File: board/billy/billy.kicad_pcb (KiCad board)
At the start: 2 copper layers, 70 x 50 mm, 85 parts, among them J1 Screw_Terminal_01x02, J10 Screw_Terminal_01x02, J11 Screw_Terminal_01x03, J12 USB_B_Micro, J2 Conn_01x06, J3 Screw_Terminal_01x02, J4 Screw_Terminal_01x02, J5 Conn_01x02, J6 Conn_01x03, J7 Screw_Terminal_01x06, Q1 AO3401A, Q2 AO3401A, Q4 AO3400A, Q6 AO3400A, Q7 AO3400A, SW1 TS-1088-AR02016, U1 ESP32-S3-WROOM-1, U2 DRV8833PWPR, U3 MAX98357A, U4 DRV8833PWPR, U5 LTC4412, U6 AP63203WU, U7 USBLC6-2SC6

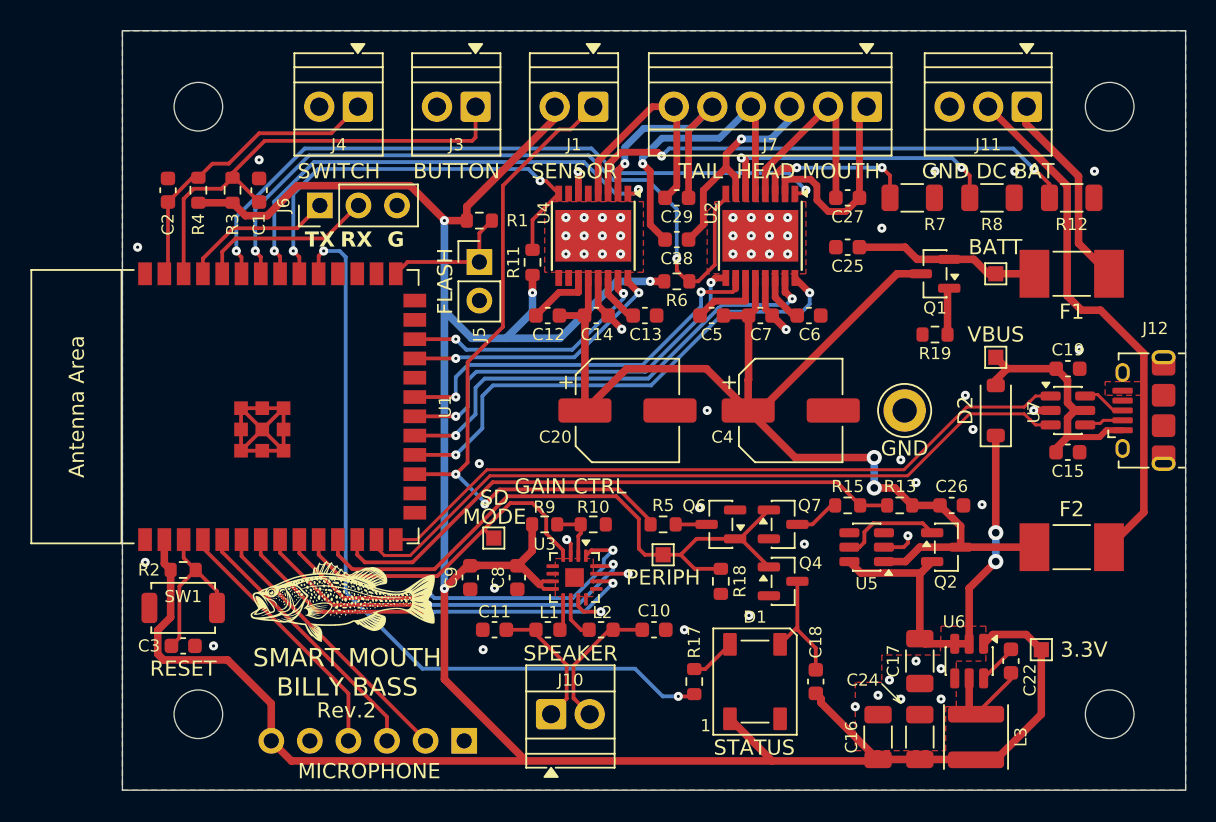
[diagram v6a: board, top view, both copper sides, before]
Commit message: Fix D2 footprint to SOD-323 (was SOD-123) and remove unused test points for rev.2
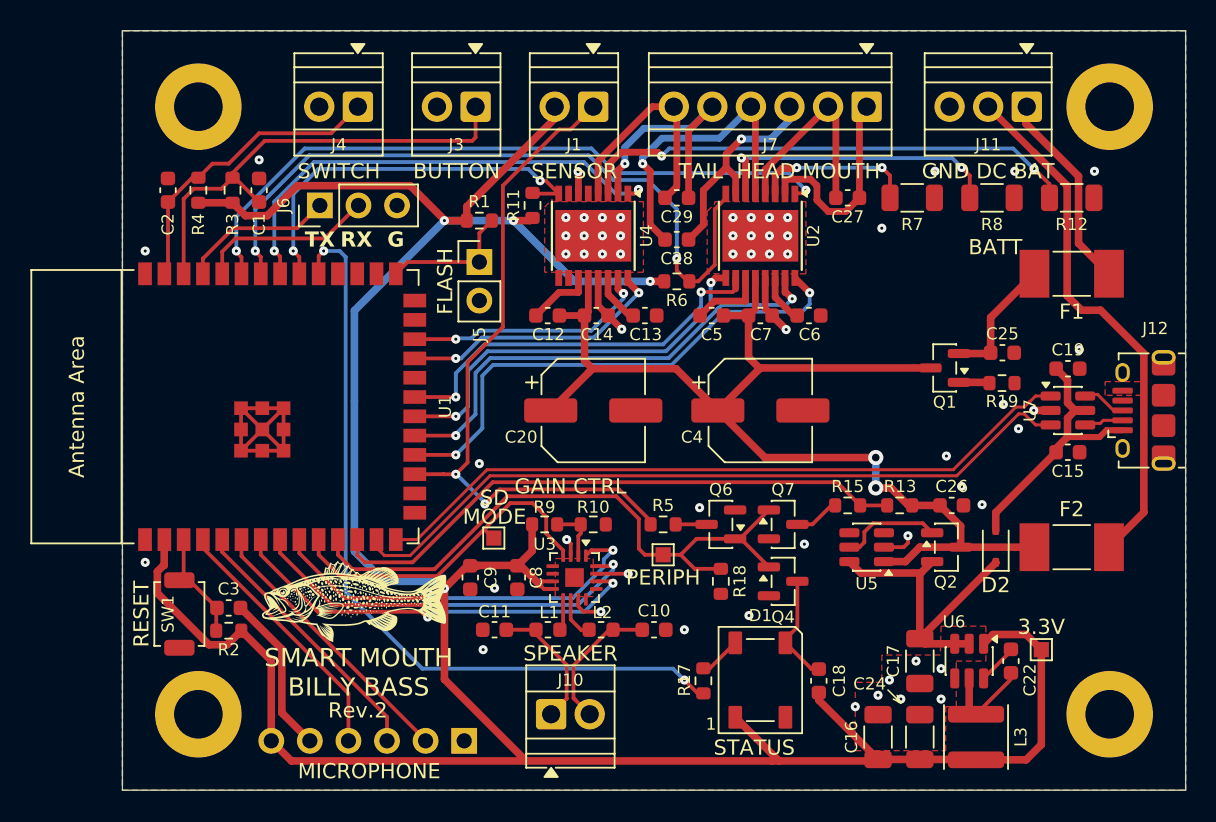
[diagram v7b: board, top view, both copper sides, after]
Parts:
- removed TP3: TestPoint, TestPoint:TestPoint_Keystone_5010-5014_Multipurpose
- removed TP5, TP6: TestPoint, TestPoint:TestPoint_Pad_1.0x1.0mm
- D2: footprint Diode_SMD:D_SOD-123 -> Diode_SMD:D_SOD-323
- H1, H2, H3, H4: footprint MountingHole:MountingHole_3.2mm_M3 -> MountingHole:MountingHole_3.2mm_M3_ISO7380_Pad
- moved C25 12.3 mm to (207.9, 71.2), turned to 0 degrees
- moved D2 8.95 mm to (207.5, 84.0)
- moved Q1 6.23 mm to (204.1, 72.2)
- moved R19 5.45 mm to (207.9, 73.2), turned to 0 degrees
- moved R2 5.00 mm to (157.0, 89.5), turned to 180 degrees
- moved C3 3.91 mm to (157.0, 88.0)
- moved R11 3.75 mm to (177.0, 61.5)
- moved C20 2.25 mm to (181.0, 75.0)
- moved C4 2.00 mm to (192.0, 75.0)
- moved G*** 0.75 mm to (165.2, 87.5)
- moved R17 0.60 mm to (188.2, 92.8)
- moved SW1 0.47 mm to (153.8, 88.4), turned to 90 degrees
- moved D1 0.36 mm to (192.0, 92.8)
- moved C18 0.21 mm to (195.8, 92.8)
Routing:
- net GND: track 37.2 -> 47.8 mm, vias 61 -> 59
- net Vdrive: track 28.2 -> 20.9 mm, vias 2 -> 0
- net +3.3V: track 190.2 -> 194.1 mm
- net +BATT: track 11.7 -> 8.50 mm
- net EN: track 11.1 -> 8.13 mm
- net GPIO39: track 28.7 -> 26.0 mm
- net Vmot: track 79.1 -> 76.5 mm
- net VBUS: track 16.7 -> 17.8 mm
- net Net-(Q1-G): track 3.10 -> 2.03 mm
- net GPIO10: track 33.5 -> 34.3 mm
- net GPIO38: track 51.0 -> 51.6 mm
- net Net-(D1-VSS): track 7.94 -> 7.29 mm
- net GPIO47: track 17.0 -> 16.4 mm
- net GPIO11: track 31.3 -> 31.9 mm
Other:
- board text removed: "GND"
- board text removed: "VBUS"
